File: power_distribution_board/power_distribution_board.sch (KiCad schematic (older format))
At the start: 29 parts

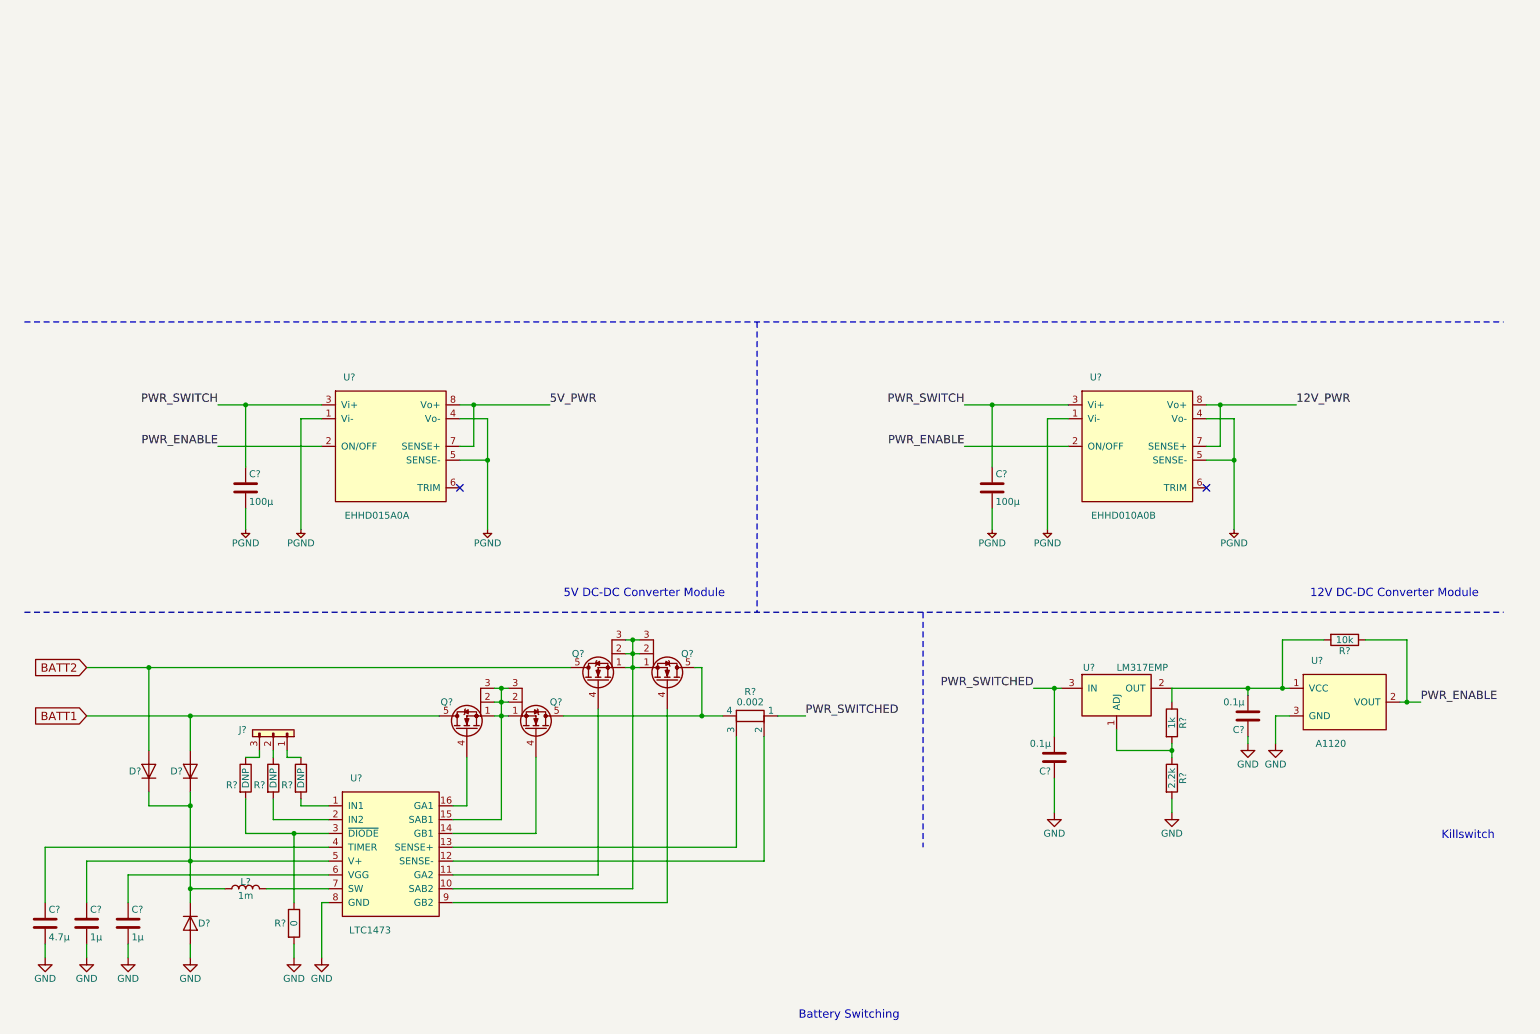
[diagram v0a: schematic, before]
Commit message: add 20V power switch
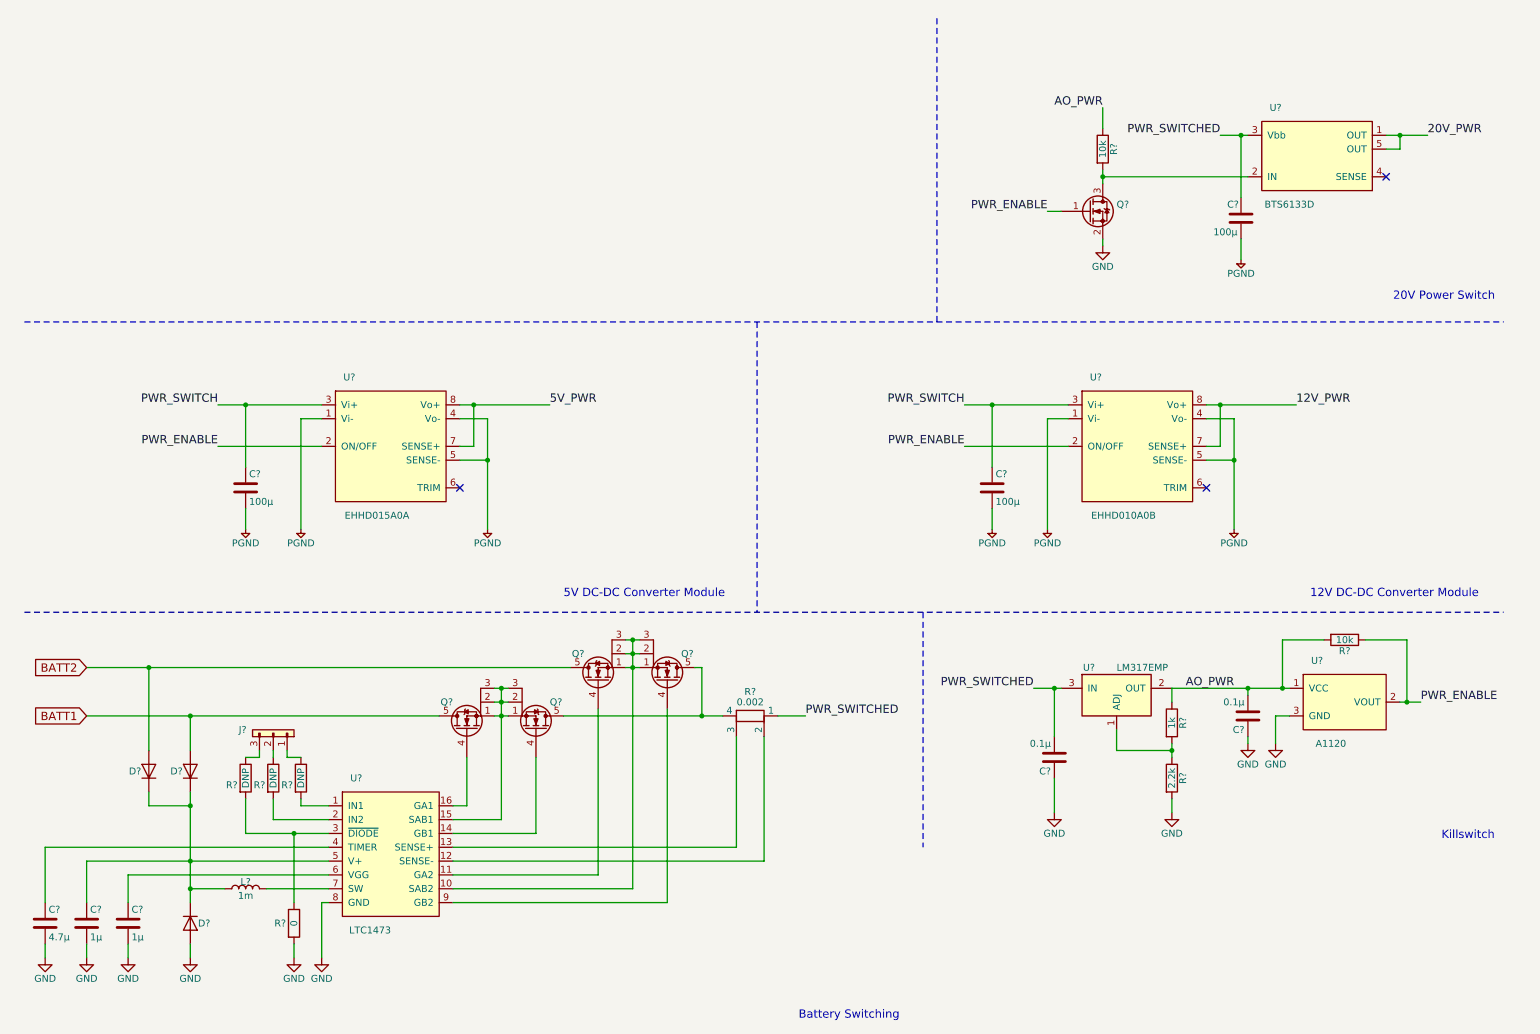
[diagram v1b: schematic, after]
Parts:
- added C?: 100μ, symbol C
- added Q?: Q_NMOS_GSD, symbol Q_NMOS_GSD
- added R?: 10k, symbol R
- added U?: BTS6133D, symbol BTS6133D
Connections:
- net GND: now also Q?.2 (S)
- net PGND: now also C?.2
- net PWR_ENABLE: now also Q?.1 (G)
- net PWR_SWITCHED: now also C?.1, U?.3 (Vbb)
- net AO_PWR: now reaches C?.2, R?.1, R?.2, U?.1 (VCC), U?.2 (OUT)
- net AO_PWR: now also R?.1
- new net: Q?.3 (D), R?.2, U?.2 (IN)
- new net 20V_PWR: U?.1 (OUT), U?.5 (OUT)
- no-connect marks 2 -> 3
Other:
- note added: "20V Power Switch"
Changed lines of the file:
@@
 $EndComp
 Wire Wire Line
-	4850 5000 4950 5000
-Wire Wire Line
-	4850 5100 4950 5100
-Wire Wire Line
-	4850 5200 4950 5200
-Wire Wire Line
-	3900 5350 4000 5350
-Wire Wire Line
-	3900 5450 4000 5450
-Wire Wire Line
-	3900 5550 4000 5550
-Wire Wire Line
-	3950 5350 3950 6300
+	4850 5000 4900 5000
+Wire Wire Line
+	4900 5000 4950 5000
+Wire Wire Line
+	4850 5100 4900 5100
+Wire Wire Line
+	4900 5100 4950 5100
+Wire Wire Line
+	4850 5200 4900 5200
+Wire Wire Line
+	4900 5200 4950 5200
+Wire Wire Line
+	3900 5350 3950 5350
+Wire Wire Line
+	3950 5350 4000 5350
+Wire Wire Line
+	3900 5450 3950 5450
+Wire Wire Line
+	3950 5450 4000 5450
+Wire Wire Line
+	3900 5550 3950 5550
+Wire Wire Line
+	3950 5550 4000 5550
+Wire Wire Line
+	3950 5350 3950 5450
+Wire Wire Line
+	3950 5450 3950 5550
+Wire Wire Line
+	3950 5550 3950 6300
 Connection ~ 3950 5450
 Connection ~ 3950 5350
 Connection ~ 3950 5550
 Wire Wire Line
-	4900 5000 4900 6800
+	4900 5000 4900 5100
+Wire Wire Line
+	4900 5100 4900 5200
+Wire Wire Line
+	4900 5200 4900 6800
 Connection ~ 4900 5200
 Wire Wire Line
 	2250 6800 2700 6800
 Wire Wire Line
-	1700 6100 1700 6900
-Wire Wire Line
-	950  6600 2700 6600
+	1700 6100 1700 6200
+Wire Wire Line
+	1700 6200 1700 6600
+Wire Wire Line
+	1700 6600 1700 6800
+Wire Wire Line
+	1700 6800 1700 6900
+Wire Wire Line
+	950  6600 1700 6600
+Wire Wire Line
+	1700 6600 2700 6600
 Connection ~ 1700 6800
 Wire Wire Line
@@
 	650  6500 650  6900
 Wire Wire Line
-	2100 6400 2700 6400
+	2100 6400 2450 6400
+Wire Wire Line
+	2450 6400 2700 6400
 Wire Wire Line
 	650  7300 650  7200
@@
 	5150 5500 5150 6900
 Wire Wire Line
-	950  5550 3500 5550
-Wire Wire Line
-	950  5200 4450 5200
+	950  5550 1700 5550
+Wire Wire Line
+	1700 5550 3500 5550
+Wire Wire Line
+	950  5200 1400 5200
+Wire Wire Line
+	1400 5200 4450 5200
 Wire Wire Line
 	1700 5800 1700 5550
@@
 Connection ~ 1400 5200
 Wire Wire Line
-	4400 5550 5550 5550
+	4400 5550 5400 5550
+Wire Wire Line
+	5400 5550 5550 5550
 Wire Wire Line
 	5350 5200 5400 5200
@@
 	2300 5850 2300 5800
 Wire Wire Line
-	8800 5350 9650 5350
+	8800 5350 9350 5350
+Wire Wire Line
+	9350 5350 9600 5350
+Wire Wire Line
+	9600 5350 9650 5350
 Wire Wire Line
 	9600 5350 9600 5000
@@
 	10500 5000 10500 5450
 Wire Wire Line
-	10450 5450 10600 5450
+	10450 5450 10500 5450
+Wire Wire Line
+	10500 5450 10600 5450
 Wire Wire Line
 	9550 5750 9550 5550
@@
 	7000 4800 7000 6500
 Wire Wire Line
-	1900 3300 2650 3300
+	1900 3300 2100 3300
+Wire Wire Line
+	2100 3300 2650 3300
 Wire Wire Line
 	2650 3400 2500 3400
@@
 	3650 3400 3850 3400
 Wire Wire Line
-	3850 3400 3850 4200
+	3850 3400 3850 3700
+Wire Wire Line
+	3850 3700 3850 4200
 Wire Wire Line
 	3650 3700 3850 3700
 Connection ~ 3850 3700
 Wire Wire Line
-	3650 3300 4300 3300
+	3650 3300 3750 3300
+Wire Wire Line
+	3750 3300 4300 3300
 Wire Wire Line
 	3650 3600 3750 3600
@@
 	1900 3600 2650 3600
 Wire Wire Line
-	7300 3300 8050 3300
+	7300 3300 7500 3300
+Wire Wire Line
+	7500 3300 8050 3300
 Wire Wire Line
 	8050 3400 7900 3400
@@
 	9050 3400 9250 3400
 Wire Wire Line
-	9250 3400 9250 4200
+	9250 3400 9250 3700
+Wire Wire Line
+	9250 3700 9250 4200
 Wire Wire Line
 	9050 3700 9250 3700
 Connection ~ 9250 3700
 Wire Wire Line
-	9050 3300 9700 3300
+	9050 3300 9150 3300
+Wire Wire Line
+	9150 3300 9700 3300
 Wire Wire Line
 	9050 3600 9150 3600
@@
 	8800 6250 8800 6150
 Wire Wire Line
-	8800 5750 8800 5850
+	8800 5750 8800 5800
+Wire Wire Line
+	8800 5800 8800 5850
 Wire Wire Line
 	8400 5650 8400 5800
@@
 Connection ~ 9350 5350
 Wire Wire Line
-	7800 5350 8000 5350
+	7800 5350 7950 5350
+Wire Wire Line
+	7950 5350 8000 5350
 Text Label 7800 5350 2    60   ~ 0
 PWR_SWITCHED
@@
 Wire Wire Line
 	7950 6250 7950 6000
+$Comp
+L BTS6133D U?
+U 1 1 598363BE
+P 9850 1450
+F 0 "U?" H 9550 1750 50  0000 C CNN
+F 1 "BTS6133D" H 9650 1050 50  0000 C CNN
+F 2 "" H 10900 1050 50  0001 C CNN
+F 3 "" H 10900 1050 50  0001 C CNN
+	1    9850 1450
+	1    0    0    -1
+$EndComp
+Wire Wire Line
+	10350 1450 10450 1450
+Wire Wire Line
+	10450 1450 10450 1350
+Wire Wire Line
+	10350 1350 10450 1350
+Wire Wire Line
+	10450 1350 10650 1350
+Connection ~ 10450 1350
+Text Label 10650 1350 0    60   ~ 0
+20V_PWR
+NoConn ~ 10350 1650
+Wire Wire Line
+	9150 1350 9300 1350
+Wire Wire Line
+	9300 1350 9350 1350
+Text Label 9150 1350 2    60   ~ 0
+PWR_SWITCHED
+$Comp
+L C C?
+U 1 1 5983DB6E
+P 9300 1950
+F 0 "C?" H 9200 2050 50  0000 L CNN
+F 1 "100μ" H 9100 1850 50  0000 L CNN
+F 2 "" H 9338 1800 50  0001 C CNN
+F 3 "" H 9300 1950 50  0001 C CNN
+	1    9300 1950
+	1    0    0    -1
+$EndComp
+Wire Wire Line
+	9300 1800 9300 1350
+Connection ~ 9300 1350
+$Comp
+L PGND #PWR?
+U 1 1 5983E640
+P 9300 2250
+F 0 "#PWR?" H 9170 2290 50  0001 L CNN
+F 1 "PGND" H 9300 2150 50  0000 C CNN
+F 2 "" H 9300 2250 60  0001 C CNN
+F 3 "" H 9300 2250 60  0001 C CNN
+	1    9300 2250
+	1    0    0    -1
+$EndComp
+Wire Wire Line
+	9300 2250 9300 2100
+Wire Wire Line
+	8300 1650 9350 1650
+$Comp
+L Q_NMOS_GSD Q?
+U 1 1 5983ED54
+P 8200 1900
+F 0 "Q?" H 8400 1950 50  0000 L CNN
+F 1 "Q_NMOS_GSD" H 8400 1850 50  0001 L CNN
+F 2 "" H 8400 2000 50  0001 C CNN
+F 3 "" H 8200 1900 50  0001 C CNN
+	1    8200 1900
+	1    0    0    -1
+$EndComp
+Text Label 8900 5350 0    60   ~ 0
+AO_PWR
+$Comp
+L R R?
+U 1 1 59841971
+P 8300 1450
+F 0 "R?" V 8380 1450 50  0000 C CNN
+F 1 "10k" V 8300 1450 50  0000 C CNN
+F 2 "" V 8230 1450 50  0001 C CNN
+F 3 "" H 8300 1450 50  0001 C CNN
+	1    8300 1450
+	1    0    0    -1
+$EndComp
+Wire Wire Line
+	8300 1600 8300 1650
+Wire Wire Line
+	8300 1650 8300 1700
+Text Label 8300 1150 2    60   ~ 0
+AO_PWR
+$Comp
+L GND #PWR?
+U 1 1 598447EB
+P 8300 2150
+F 0 "#PWR?" H 8300 1900 50  0001 C CNN
+F 1 "GND" H 8300 2000 50  0000 C CNN
+F 2 "" H 8300 2150 50  0001 C CNN
+F 3 "" H 8300 2150 50  0001 C CNN
+	1    8300 2150
+	1    0    0    -1
+$EndComp
+Wire Wire Line
+	8300 2150 8300 2100
+Wire Wire Line
+	7900 1900 8000 1900
+Text Label 7900 1900 2    60   ~ 0
+PWR_ENABLE
+Connection ~ 8300 1650
+Wire Wire Line
+	8300 1300 8300 1150
+Wire Notes Line
+	7100 2700 7100 500
+Text Notes 10400 2550 0    60   ~ 0
+20V Power Switch
 $EndSCHEMATC

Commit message: add diagnostic LEDs
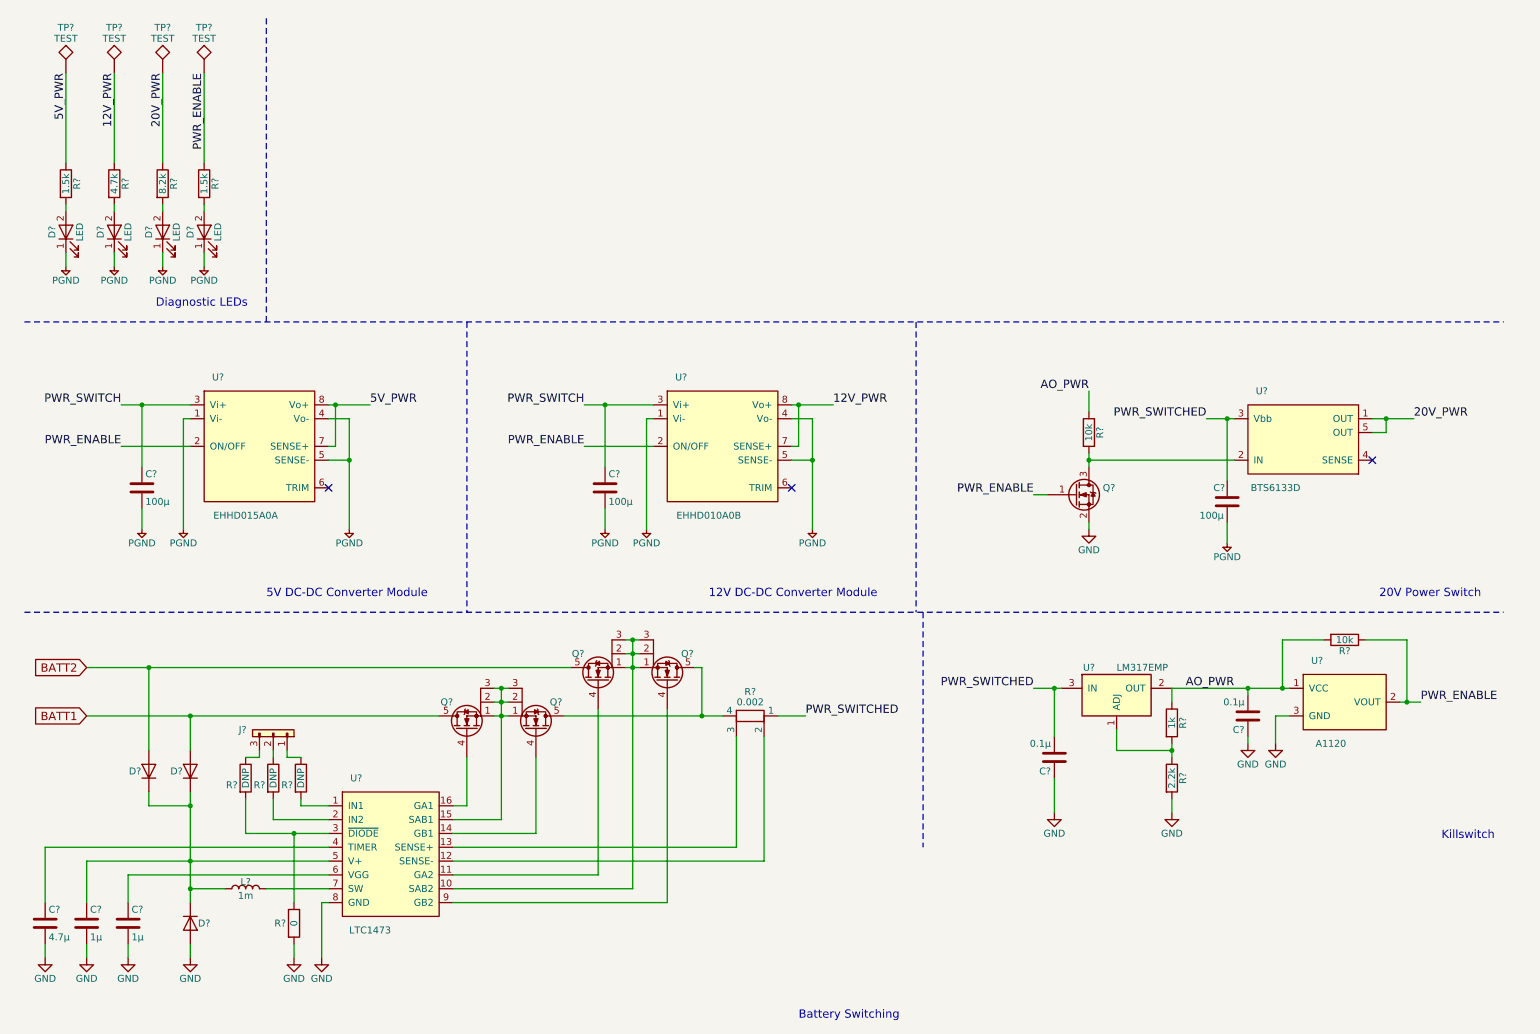
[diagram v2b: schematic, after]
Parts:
- added D? (x4): LED, symbol LED
- added R? (x2): 1.5k, symbol R
- added R?: 4.7k, symbol R
- added R?: 8.2k, symbol R
- added TP? (x4): TEST, symbol TEST
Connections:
- net 12V_PWR: now also R?.1, TP?.1
- net 20V_PWR: now also R?.1, TP?.1
- net 5V_PWR: now also R?.1, TP?.1
- net PGND: now also D?.1 (K), D?.1 (K), D?.1 (K), D?.1 (K)
- net PWR_ENABLE: now also R?.1, TP?.1
- new net: D?.2 (A), R?.2 (x4)
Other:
- note added: "Diagnostic LEDs"
- moved on the sheet: C?, Q?, R?, U?

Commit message: add connectors
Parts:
- added J? (x20): CONN_02X01, symbol CONN_02X01
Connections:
- net PGND is gone; now on net GND: C?.2, C?.2, C?.2, D?.1 (K), D?.1 (K), D?.1 (K), D?.1 (K), U?.1 (Vi-), U?.1 (Vi-), U?.4 (Vo-), U?.4 (Vo-), U?.5 (SENSE-), U?.5 (SENSE-)
- net 12V_PWR: now also J?.1 (P1), J?.1 (P1), J?.1 (P1), J?.1 (P1), J?.1 (P1), J?.1 (P1), J?.1 (P1), J?.1 (P1), J?.1 (P1), J?.1 (P1)
- net 20V_PWR: now also J?.1 (P1), J?.1 (P1), J?.1 (P1), J?.1 (P1)
- net 5V_PWR: now also J?.1 (P1), J?.1 (P1), J?.1 (P1), J?.1 (P1), J?.1 (P1), J?.1 (P1)
- net GND: now also J?.2 (P2), J?.2 (P2), J?.2 (P2), J?.2 (P2), J?.2 (P2), J?.2 (P2), J?.2 (P2), J?.2 (P2), J?.2 (P2), J?.2 (P2), J?.2 (P2), J?.2 (P2), J?.2 (P2), J?.2 (P2), J?.2 (P2), J?.2 (P2), J?.2 (P2), J?.2 (P2), J?.2 (P2), J?.2 (P2)
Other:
- note added: "Connectors"
- note added: "Jetson"
- note added: "Light Board"
- note added: "Motor Controller"
- note added: "Motors"
- note added: "Pressure Sensor"
- note added: "Raspberry Pi"
- note added: "Sonar"
- note added: "Spare 12V"
- note added: "Spare 20V"
- note added: "Spare 5V"

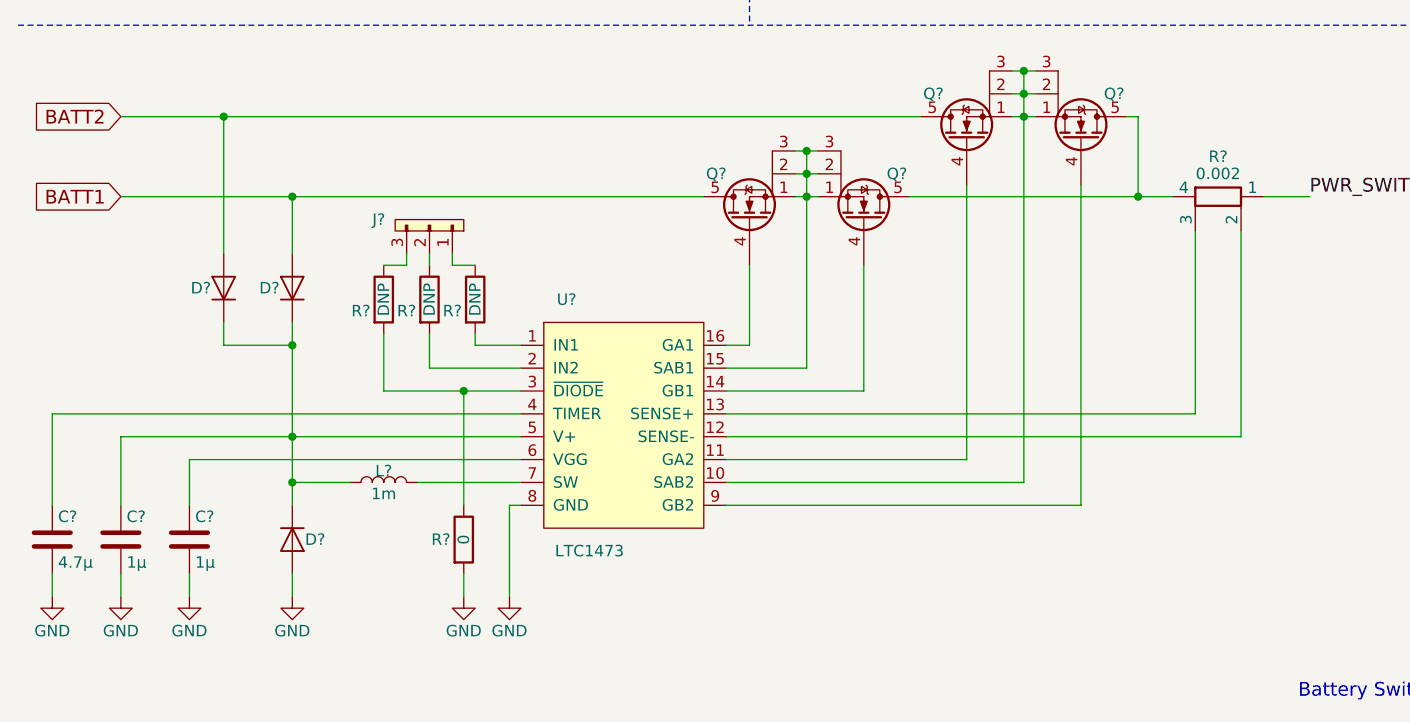
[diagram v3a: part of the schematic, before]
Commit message: update component values for battery switching
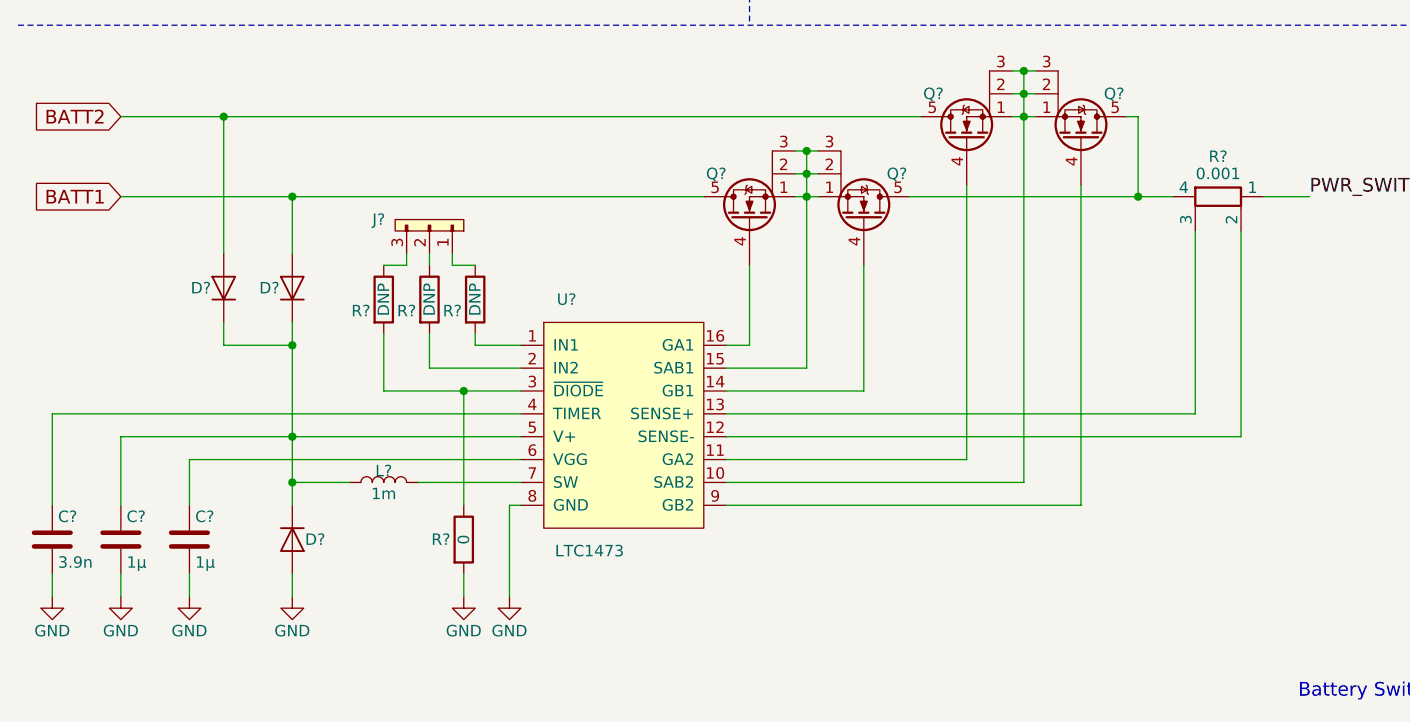
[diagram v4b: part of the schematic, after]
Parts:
- C?: value 4.7μ -> 3.9n
- R?: value 0.002 -> 0.001
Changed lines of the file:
@@
 P 650 7050
 F 0 "C?" H 675 7150 50  0000 L CNN
-F 1 "4.7μ" H 675 6950 50  0000 L CNN
+F 1 "3.9n" H 675 6950 50  0000 L CNN
 F 2 "" H 688 6900 50  0001 C CNN
 F 3 "" H 650 7050 50  0001 C CNN
@@
 P 5750 5550
 F 0 "R?" V 5575 5550 50  0000 C CNN
-F 1 "0.002" V 5650 5550 50  0000 C CNN
+F 1 "0.001" V 5650 5550 50  0000 C CNN
 F 2 "" V 5680 5550 50  0001 C CNN
 F 3 "" H 5750 5550 50  0001 C CNN
